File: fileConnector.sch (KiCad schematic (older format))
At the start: 7 parts, among them J2 TE_Eurocard_96pole

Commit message: Renaming files, cleaning, CHANGELOG
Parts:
- renumbered C30 to C?, C31 to C?, D1 to D?, D2 to D?, J2 to J?, R4 to R?, R5 to R?
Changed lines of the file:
@@
 $Descr A4 11693 8268
 encoding utf-8
-Sheet 5 8
+Sheet 8 8
 Title "GP8B"
 Date "2019-05-12"
@@
 BWRITE2_7
 $Comp
-L power:GND #PWR072
+L power:GND #PWR?
 U 1 1 5B172ED1
 P 5900 7450
-F 0 "#PWR072" H 5900 7200 50  0001 C CNN
+F 0 "#PWR?" H 5900 7200 50  0001 C CNN
 F 1 "GND" H 5900 7300 50  0000 C CNN
 F 2 "" H 5900 7450 50  0001 C CNN
@@
 $EndComp
 $Comp
-L power:+5V #PWR073
+L power:+5V #PWR?
 U 1 1 5B173077
 P 6400 6850
-F 0 "#PWR073" H 6400 6700 50  0001 C CNN
+F 0 "#PWR?" H 6400 6700 50  0001 C CNN
 F 1 "+5V" H 6400 6990 50  0000 C CNN
 F 2 "" H 6400 6850 50  0001 C CNN
@@
 GLOBAL_CLK
 $Comp
-L Device:R R4
+L Device:R R?
 U 1 1 5B1B85C4
 P 3150 6100
-F 0 "R4" V 3230 6100 50  0000 C CNN
+F 0 "R?" V 3230 6100 50  0000 C CNN
 F 1 "1k5" V 3150 6100 50  0000 C CNN
 F 2 "Resistor_SMD:R_0805_2012Metric" V 3080 6100 50  0001 C CNN
@@
 $EndComp
 $Comp
-L Device:LED D1
+L Device:LED D?
 U 1 1 5B1B85CB
 P 3150 6600
-F 0 "D1" H 3150 6700 50  0000 C CNN
+F 0 "D?" H 3150 6700 50  0000 C CNN
 F 1 "GREEN_2.65V_2mA" H 3150 6450 50  0000 C CNN
 F 2 "LED_SMD:LED_1206_3216Metric" H 3150 6600 50  0001 C CNN
@@
 $EndComp
 $Comp
-L power:+5V #PWR074
+L power:+5V #PWR?
 U 1 1 5B1B85D2
 P 3150 5850
-F 0 "#PWR074" H 3150 5700 50  0001 C CNN
+F 0 "#PWR?" H 3150 5700 50  0001 C CNN
 F 1 "+5V" H 3150 5990 50  0000 C CNN
 F 2 "" H 3150 5850 50  0001 C CNN
@@
 $EndComp
 $Comp
-L power:GND #PWR075
+L power:GND #PWR?
 U 1 1 5B1B85D8
 P 3150 6850
-F 0 "#PWR075" H 3150 6600 50  0001 C CNN
+F 0 "#PWR?" H 3150 6600 50  0001 C CNN
 F 1 "GND" H 3150 6700 50  0000 C CNN
 F 2 "" H 3150 6850 50  0001 C CNN
@@
 	3150 6750 3150 6850
 $Comp
-L power:+3.3V #PWR076
+L power:+3.3V #PWR?
 U 1 1 5B0EADF6
 P 6150 6750
-F 0 "#PWR076" H 6150 6600 50  0001 C CNN
+F 0 "#PWR?" H 6150 6600 50  0001 C CNN
 F 1 "+3.3V" H 6150 6890 50  0000 C CNN
 F 2 "" H 6150 6750 50  0001 C CNN
@@
 $EndComp
 $Comp
-L Device:C C30
+L Device:C C?
 U 1 1 5B0EB326
 P 6150 7200
-F 0 "C30" H 6175 7300 50  0000 L CNN
+F 0 "C?" H 6175 7300 50  0000 L CNN
 F 1 "10nF" H 6175 7100 50  0000 L CNN
 F 2 "Capacitor_SMD:C_0805_2012Metric" H 6188 7050 50  0001 C CNN
@@
 $EndComp
 $Comp
-L Device:C C31
+L Device:C C?
 U 1 1 5B0EB41C
 P 6400 7200
-F 0 "C31" H 6425 7300 50  0000 L CNN
+F 0 "C?" H 6425 7300 50  0000 L CNN
 F 1 "10nF" H 6425 7100 50  0000 L CNN
 F 2 "Capacitor_SMD:C_0805_2012Metric" H 6438 7050 50  0001 C CNN
@@
 	5900 7000 5900 7400
 $Comp
-L power:PWR_FLAG #FLG077
+L power:PWR_FLAG #FLG?
 U 1 1 5B0E568B
 P 6700 6600
-F 0 "#FLG077" H 6700 6675 50  0001 C CNN
+F 0 "#FLG?" H 6700 6675 50  0001 C CNN
 F 1 "PWR_FLAG" H 6700 6750 50  0000 C CNN
 F 2 "" H 6700 6600 50  0001 C CNN
@@
 $EndComp
 $Comp
-L power:PWR_FLAG #FLG078
+L power:PWR_FLAG #FLG?
 U 1 1 5B0E576E
 P 6300 6600
-F 0 "#FLG078" H 6300 6675 50  0001 C CNN
+F 0 "#FLG?" H 6300 6675 50  0001 C CNN
 F 1 "PWR_FLAG" H 6300 6750 50  0000 C CNN
 F 2 "" H 6300 6600 50  0001 C CNN
@@
 $EndComp
 $Comp
-L power:PWR_FLAG #FLG079
+L power:PWR_FLAG #FLG?
 U 1 1 5B0E81E2
 P 6750 7300
-F 0 "#FLG079" H 6750 7375 50  0001 C CNN
+F 0 "#FLG?" H 6750 7375 50  0001 C CNN
 F 1 "PWR_FLAG" H 6750 7450 50  0000 C CNN
 F 2 "" H 6750 7300 50  0001 C CNN
@@
 BREAD2_[0..7]
 $Comp
-L power:+3.3V #PWR080
+L power:+3.3V #PWR?
 U 1 1 5B21A313
 P 3700 5850
-F 0 "#PWR080" H 3700 5700 50  0001 C CNN
+F 0 "#PWR?" H 3700 5700 50  0001 C CNN
 F 1 "+3.3V" H 3700 5990 50  0000 C CNN
 F 2 "" H 3700 5850 50  0001 C CNN
@@
 $EndComp
 $Comp
-L Device:R R5
+L Device:R R?
 U 1 1 5B21A4F8
 P 3700 6100
-F 0 "R5" V 3780 6100 50  0000 C CNN
+F 0 "R?" V 3780 6100 50  0000 C CNN
 F 1 "470E" V 3700 6100 50  0000 C CNN
 F 2 "Resistor_SMD:R_0805_2012Metric" V 3630 6100 50  0001 C CNN
@@
 $EndComp
 $Comp
-L power:GND #PWR081
+L power:GND #PWR?
 U 1 1 5B21A504
 P 3700 6850
-F 0 "#PWR081" H 3700 6600 50  0001 C CNN
+F 0 "#PWR?" H 3700 6600 50  0001 C CNN
 F 1 "GND" H 3700 6700 50  0000 C CNN
 F 2 "" H 3700 6850 50  0001 C CNN
@@
 	3700 6750 3700 6850
 $Comp
-L Device:LED D2
+L Device:LED D?
 U 1 1 5B21A63F
 P 3700 6600
-F 0 "D2" H 3700 6700 50  0000 C CNN
+F 0 "D?" H 3700 6700 50  0000 C CNN
 F 1 "GREEN_2.65V_2mA" H 3700 6450 50  0000 C CNN
 F 2 "LED_SMD:LED_1206_3216Metric" H 3700 6600 50  0001 C CNN
@@
 	6400 7400 6750 7400
 $Comp
-L Custom:TE_Eurocard_96pole J2
+L Custom:TE_Eurocard_96pole J?
 U 1 1 5C9A234B
 P 5300 4600
-F 0 "J2" H 5300 7115 50  0000 C CNN
+F 0 "J?" H 5300 7115 50  0000 C CNN
 F 1 "TE_Eurocard_96pole" H 5300 7024 50  0000 C CNN
 F 2 "Eurocard_5536475-1:Eurocard_5536475-1" H 5250 5000 50  0001 C CNN
@@
 SPI_MISO
 $Comp
-L power:+5V #PWR0132
+L power:+5V #PWR?
 U 1 1 5DEF449C
 P 6550 3650
-F 0 "#PWR0132" H 6550 3500 50  0001 C CNN
+F 0 "#PWR?" H 6550 3500 50  0001 C CNN
 F 1 "+5V" H 6550 3790 50  0000 C CNN
 F 2 "" H 6550 3650 50  0001 C CNN

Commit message: Cleaning
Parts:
- gave numbers to parts that had none: 7
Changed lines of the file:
@@
 BWRITE2_7
 $Comp
-L power:GND #PWR?
+L power:GND #PWR0146
 U 1 1 5B172ED1
 P 5900 7450
-F 0 "#PWR?" H 5900 7200 50  0001 C CNN
+F 0 "#PWR0146" H 5900 7200 50  0001 C CNN
 F 1 "GND" H 5900 7300 50  0000 C CNN
 F 2 "" H 5900 7450 50  0001 C CNN
@@
 $EndComp
 $Comp
-L power:+5V #PWR?
+L power:+5V #PWR0147
 U 1 1 5B173077
 P 6400 6850
-F 0 "#PWR?" H 6400 6700 50  0001 C CNN
+F 0 "#PWR0147" H 6400 6700 50  0001 C CNN
 F 1 "+5V" H 6400 6990 50  0000 C CNN
 F 2 "" H 6400 6850 50  0001 C CNN
@@
 GLOBAL_CLK
 $Comp
-L Device:R R?
+L Device:R R4
 U 1 1 5B1B85C4
 P 3150 6100
-F 0 "R?" V 3230 6100 50  0000 C CNN
+F 0 "R4" V 3230 6100 50  0000 C CNN
 F 1 "1k5" V 3150 6100 50  0000 C CNN
 F 2 "Resistor_SMD:R_0805_2012Metric" V 3080 6100 50  0001 C CNN
@@
 $EndComp
 $Comp
-L Device:LED D?
+L Device:LED D1
 U 1 1 5B1B85CB
 P 3150 6600
-F 0 "D?" H 3150 6700 50  0000 C CNN
+F 0 "D1" H 3150 6700 50  0000 C CNN
 F 1 "GREEN_2.65V_2mA" H 3150 6450 50  0000 C CNN
 F 2 "LED_SMD:LED_1206_3216Metric" H 3150 6600 50  0001 C CNN
@@
 $EndComp
 $Comp
-L power:+5V #PWR?
+L power:+5V #PWR0148
 U 1 1 5B1B85D2
 P 3150 5850
-F 0 "#PWR?" H 3150 5700 50  0001 C CNN
+F 0 "#PWR0148" H 3150 5700 50  0001 C CNN
 F 1 "+5V" H 3150 5990 50  0000 C CNN
 F 2 "" H 3150 5850 50  0001 C CNN
@@
 $EndComp
 $Comp
-L power:GND #PWR?
+L power:GND #PWR0149
 U 1 1 5B1B85D8
 P 3150 6850
-F 0 "#PWR?" H 3150 6600 50  0001 C CNN
+F 0 "#PWR0149" H 3150 6600 50  0001 C CNN
 F 1 "GND" H 3150 6700 50  0000 C CNN
 F 2 "" H 3150 6850 50  0001 C CNN
@@
 	3150 6750 3150 6850
 $Comp
-L power:+3.3V #PWR?
+L power:+3.3V #PWR0150
 U 1 1 5B0EADF6
 P 6150 6750
-F 0 "#PWR?" H 6150 6600 50  0001 C CNN
+F 0 "#PWR0150" H 6150 6600 50  0001 C CNN
 F 1 "+3.3V" H 6150 6890 50  0000 C CNN
 F 2 "" H 6150 6750 50  0001 C CNN
@@
 $EndComp
 $Comp
-L Device:C C?
+L Device:C C30
 U 1 1 5B0EB326
 P 6150 7200
-F 0 "C?" H 6175 7300 50  0000 L CNN
+F 0 "C30" H 6175 7300 50  0000 L CNN
 F 1 "10nF" H 6175 7100 50  0000 L CNN
 F 2 "Capacitor_SMD:C_0805_2012Metric" H 6188 7050 50  0001 C CNN
@@
 $EndComp
 $Comp
-L Device:C C?
+L Device:C C31
 U 1 1 5B0EB41C
 P 6400 7200
-F 0 "C?" H 6425 7300 50  0000 L CNN
+F 0 "C31" H 6425 7300 50  0000 L CNN
 F 1 "10nF" H 6425 7100 50  0000 L CNN
 F 2 "Capacitor_SMD:C_0805_2012Metric" H 6438 7050 50  0001 C CNN
@@
 	5900 7000 5900 7400
 $Comp
-L power:PWR_FLAG #FLG?
+L power:PWR_FLAG #FLG0101
 U 1 1 5B0E568B
 P 6700 6600
-F 0 "#FLG?" H 6700 6675 50  0001 C CNN
+F 0 "#FLG0101" H 6700 6675 50  0001 C CNN
 F 1 "PWR_FLAG" H 6700 6750 50  0000 C CNN
 F 2 "" H 6700 6600 50  0001 C CNN
@@
 $EndComp
 $Comp
-L power:PWR_FLAG #FLG?
+L power:PWR_FLAG #FLG0102
 U 1 1 5B0E576E
 P 6300 6600
-F 0 "#FLG?" H 6300 6675 50  0001 C CNN
+F 0 "#FLG0102" H 6300 6675 50  0001 C CNN
 F 1 "PWR_FLAG" H 6300 6750 50  0000 C CNN
 F 2 "" H 6300 6600 50  0001 C CNN
@@
 $EndComp
 $Comp
-L power:PWR_FLAG #FLG?
+L power:PWR_FLAG #FLG0103
 U 1 1 5B0E81E2
 P 6750 7300
-F 0 "#FLG?" H 6750 7375 50  0001 C CNN
+F 0 "#FLG0103" H 6750 7375 50  0001 C CNN
 F 1 "PWR_FLAG" H 6750 7450 50  0000 C CNN
 F 2 "" H 6750 7300 50  0001 C CNN
@@
 BREAD2_[0..7]
 $Comp
-L power:+3.3V #PWR?
+L power:+3.3V #PWR0151
 U 1 1 5B21A313
 P 3700 5850
-F 0 "#PWR?" H 3700 5700 50  0001 C CNN
+F 0 "#PWR0151" H 3700 5700 50  0001 C CNN
 F 1 "+3.3V" H 3700 5990 50  0000 C CNN
 F 2 "" H 3700 5850 50  0001 C CNN
@@
 $EndComp
 $Comp
-L Device:R R?
+L Device:R R5
 U 1 1 5B21A4F8
 P 3700 6100
-F 0 "R?" V 3780 6100 50  0000 C CNN
+F 0 "R5" V 3780 6100 50  0000 C CNN
 F 1 "470E" V 3700 6100 50  0000 C CNN
 F 2 "Resistor_SMD:R_0805_2012Metric" V 3630 6100 50  0001 C CNN
@@
 $EndComp
 $Comp
-L power:GND #PWR?
+L power:GND #PWR0152
 U 1 1 5B21A504
 P 3700 6850
-F 0 "#PWR?" H 3700 6600 50  0001 C CNN
+F 0 "#PWR0152" H 3700 6600 50  0001 C CNN
 F 1 "GND" H 3700 6700 50  0000 C CNN
 F 2 "" H 3700 6850 50  0001 C CNN
@@
 	3700 6750 3700 6850
 $Comp
-L Device:LED D?
+L Device:LED D2
 U 1 1 5B21A63F
 P 3700 6600
-F 0 "D?" H 3700 6700 50  0000 C CNN
+F 0 "D2" H 3700 6700 50  0000 C CNN
 F 1 "GREEN_2.65V_2mA" H 3700 6450 50  0000 C CNN
 F 2 "LED_SMD:LED_1206_3216Metric" H 3700 6600 50  0001 C CNN
@@
 	6400 7400 6750 7400
 $Comp
-L Custom:TE_Eurocard_96pole J?
+L Custom:TE_Eurocard_96pole J2
 U 1 1 5C9A234B
 P 5300 4600
-F 0 "J?" H 5300 7115 50  0000 C CNN
+F 0 "J2" H 5300 7115 50  0000 C CNN
 F 1 "TE_Eurocard_96pole" H 5300 7024 50  0000 C CNN
 F 2 "Eurocard_5536475-1:Eurocard_5536475-1" H 5250 5000 50  0001 C CNN
@@
 SPI_MISO
 $Comp
-L power:+5V #PWR?
+L power:+5V #PWR0153
 U 1 1 5DEF449C
 P 6550 3650
-F 0 "#PWR?" H 6550 3500 50  0001 C CNN
+F 0 "#PWR0153" H 6550 3500 50  0001 C CNN
 F 1 "+5V" H 6550 3790 50  0000 C CNN
 F 2 "" H 6550 3650 50  0001 C CNN

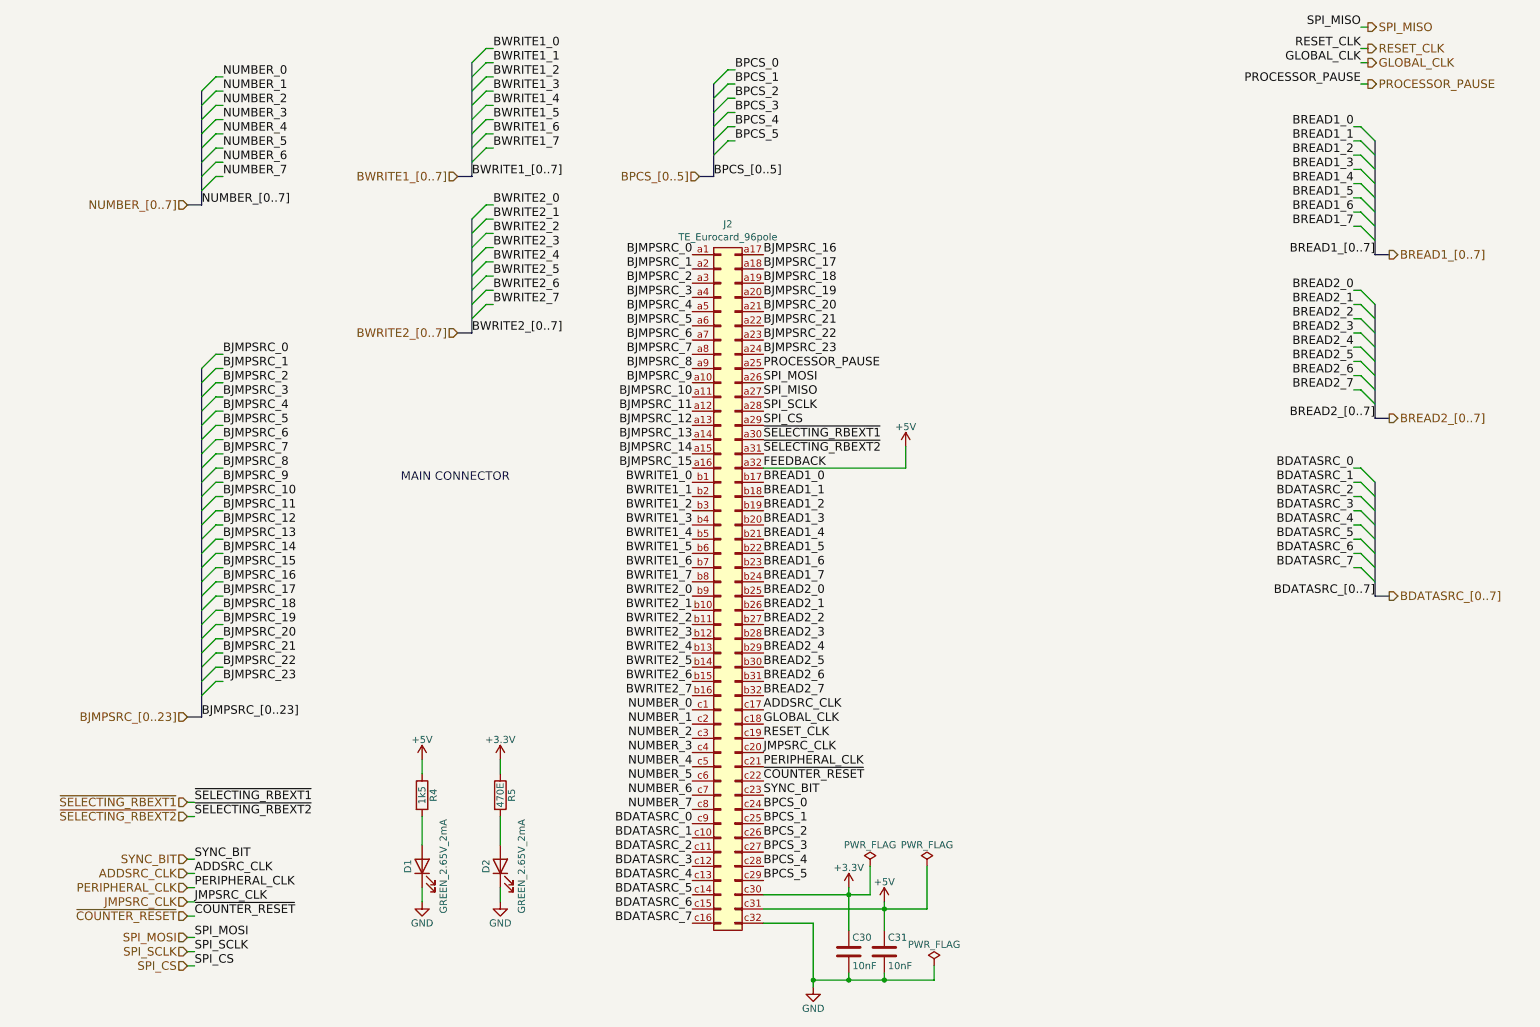
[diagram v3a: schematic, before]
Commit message: V5.1 (#9)
* Apply new symbol for XC2C256-VQ100 #5

* Set new date and 5.1

* Replacing 74HC165 with 74HC166, and add SPI_CFG_DS #4

* Replace some gates with a 74AHC1G02 to fix the pulse problem #3

* Go next only if SRCVALUE, (simple instruction)

* Remove weird ghost bus in register

* Small cleaning in fileRegister

* Go next only if SRCVALUE, (complex instruction) #8
adding 74AHC1G08

* Better decoupling #6

* Component association (#7)

* netlist

* Updated BOM for V5.1

* Routing, cleaning first pass

* bit of pcb cleaning

* SolderMaskClearance to 0

* Schematics to pdf

* PCB files in pdf

* exporting Gerbert files

* new 3d images

* Update README.md

* Modifying CHANGELOG file

* Update README.md
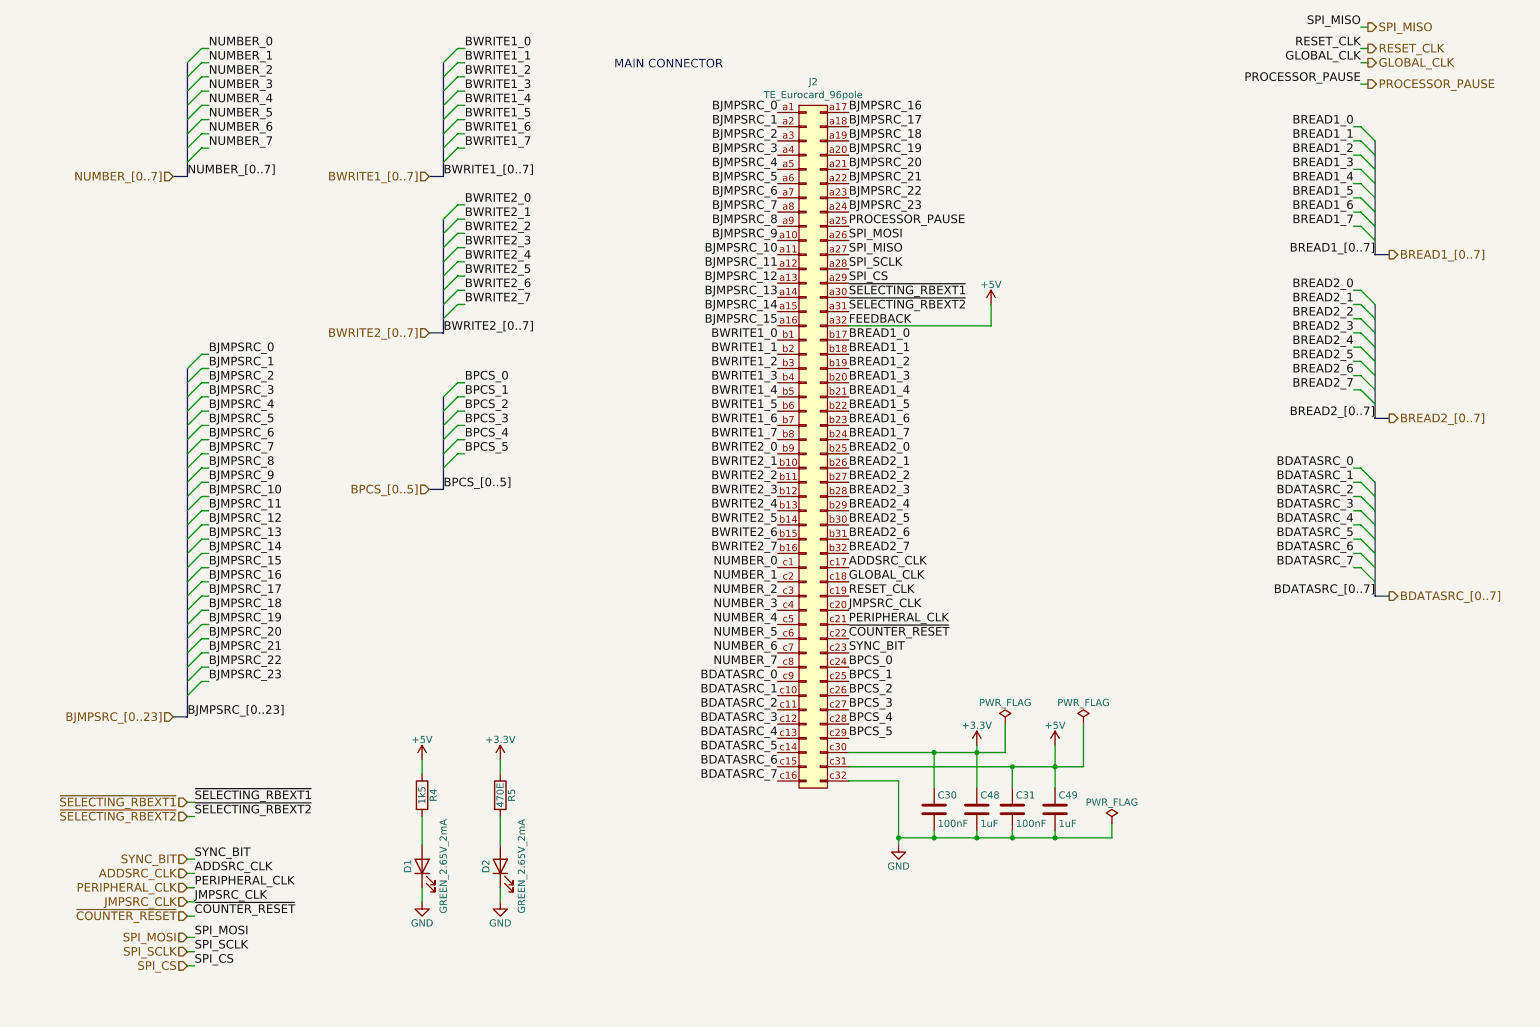
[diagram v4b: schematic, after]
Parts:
- added C48, C49: 1uF, Capacitor_SMD:C_0805_2012Metric, symbol Device:C
- C30, C31: value 10nF -> 100nF
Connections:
- net +3V3: now also C48.1
- net +5V: now also C49.1
- net GND: now also C48.2, C49.2
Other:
- moved on the sheet: C30, C31, J2
